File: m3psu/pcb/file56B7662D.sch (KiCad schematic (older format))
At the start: 12 parts

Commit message: Finished passives for Li-ion Charger. Tweaked and cleaned up values in DC/DC Converter.
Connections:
- wire segments 209 -> 164
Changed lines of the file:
@@
 	2250 3600 2200 3600
 Wire Wire Line
-	2250 3300 2250 3400
-Wire Wire Line
-	2250 3400 2250 3500
-Wire Wire Line
-	2250 3500 2250 3600
-Wire Wire Line
-	2250 3600 2250 3700
+	2250 3300 2250 3700
 Wire Wire Line
 	2200 3300 2250 3300
@@
 Connection ~ 950  2400
 Wire Wire Line
-	850  2400 950  2400
-Wire Wire Line
-	950  2400 1000 2400
+	850  2400 1000 2400
 Connection ~ 950  2300
 Wire Wire Line
@@
 	1000 2200 950  2200
 Wire Wire Line
-	950  2100 950  2200
-Wire Wire Line
-	950  2200 950  2300
-Wire Wire Line
-	950  2300 950  2400
-Wire Wire Line
-	950  2400 950  2500
-Wire Wire Line
-	950  2500 950  2600
-Wire Wire Line
-	950  2600 950  2800
+	950  2100 950  2800
 Wire Wire Line
 	950  2600 1000 2600
@@
 	800  3600 1000 3600
 Wire Wire Line
-	800  3350 800  3400
-Wire Wire Line
-	800  3400 800  3600
+	800  3350 800  3600
 Wire Wire Line
 	1000 3400 950  3400
@@
 	800  3100 1000 3100
 Wire Wire Line
-	800  1400 800  1550
-Wire Wire Line
-	800  1550 800  1850
-Wire Wire Line
-	800  1850 800  3100
+	800  1400 800  3100
 Wire Wire Line
 	800  1550 900  1550
@@
 	900  1650 750  1650
 Wire Wire Line
-	750  1500 750  1650
-Wire Wire Line
-	750  1650 750  1900
-Wire Wire Line
-	750  1900 750  2900
-Wire Wire Line
-	750  2900 750  3200
+	750  1500 750  3200
 Wire Wire Line
 	750  3200 1000 3200
@@
 	6750 3600 6700 3600
 Wire Wire Line
-	6750 3300 6750 3400
-Wire Wire Line
-	6750 3400 6750 3500
-Wire Wire Line
-	6750 3500 6750 3600
-Wire Wire Line
-	6750 3600 6750 3700
+	6750 3300 6750 3700
 Wire Wire Line
 	6700 3300 6750 3300
@@
 Connection ~ 5450 2400
 Wire Wire Line
-	5350 2400 5450 2400
-Wire Wire Line
-	5450 2400 5500 2400
+	5350 2400 5500 2400
 Connection ~ 5450 2300
 Wire Wire Line
@@
 	5300 3600 5500 3600
 Wire Wire Line
-	5300 3350 5300 3400
-Wire Wire Line
-	5300 3400 5300 3600
+	5300 3350 5300 3600
 Wire Wire Line
 	5500 3400 5450 3400
@@
 	5300 3100 5500 3100
 Wire Wire Line
-	5300 1400 5300 1550
-Wire Wire Line
-	5300 1550 5300 1850
-Wire Wire Line
-	5300 1850 5300 3100
+	5300 1400 5300 3100
 Wire Wire Line
 	5300 1550 5400 1550
@@
 	5400 1650 5250 1650
 Wire Wire Line
-	5250 1500 5250 1650
-Wire Wire Line
-	5250 1650 5250 1900
-Wire Wire Line
-	5250 1900 5250 2800
-Wire Wire Line
-	5250 2800 5250 2900
-Wire Wire Line
-	5250 2900 5250 3200
+	5250 1500 5250 3200
 Wire Wire Line
 	5250 3200 5500 3200
@@
 	2250 7250 2200 7250
 Wire Wire Line
-	2250 6950 2250 7050
-Wire Wire Line
-	2250 7050 2250 7150
-Wire Wire Line
-	2250 7150 2250 7250
-Wire Wire Line
-	2250 7250 2250 7350
+	2250 6950 2250 7350
 Wire Wire Line
 	2200 6950 2250 6950
@@
 Connection ~ 950  6050
 Wire Wire Line
-	850  6050 950  6050
-Wire Wire Line
-	950  6050 1000 6050
+	850  6050 1000 6050
 Connection ~ 950  5950
 Wire Wire Line
@@
 	1000 5850 950  5850
 Wire Wire Line
-	950  5750 950  5850
-Wire Wire Line
-	950  5850 950  5950
-Wire Wire Line
-	950  5950 950  6050
-Wire Wire Line
-	950  6050 950  6150
-Wire Wire Line
-	950  6150 950  6250
-Wire Wire Line
-	950  6250 950  6450
+	950  5750 950  6450
 Wire Wire Line
 	800  7250 1000 7250
 Wire Wire Line
-	800  7000 800  7050
-Wire Wire Line
-	800  7050 800  7250
+	800  7000 800  7250
 Wire Wire Line
 	1000 7050 950  7050
@@
 	800  6750 1000 6750
 Wire Wire Line
-	800  5050 800  5200
-Wire Wire Line
-	800  5200 800  5500
-Wire Wire Line
-	800  5500 800  6750
+	800  5050 800  6750
 Wire Wire Line
 	800  5200 900  5200
@@
 	900  5300 750  5300
 Wire Wire Line
-	750  5150 750  5300
-Wire Wire Line
-	750  5300 750  5550
-Wire Wire Line
-	750  5550 750  6550
-Wire Wire Line
-	750  6550 750  6850
+	750  5150 750  6850
 Wire Wire Line
 	750  6850 1000 6850
@@
 	850  6250 850  6200
 Wire Wire Line
-	5450 2100 5450 2200
-Wire Wire Line
-	5450 2200 5450 2300
-Wire Wire Line
-	5450 2300 5450 2400
-Wire Wire Line
-	5450 2400 5450 2500
-Wire Wire Line
-	5450 2500 5450 2600
+	5450 2100 5450 2600
 Wire Wire Line
 	5500 2800 5250 2800

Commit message: Linked the footprints to some parts. Cleaned up a little more of DC/DC Converter.
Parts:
- R? (x3): value 1K -> 1k
- R? (x3): value 100K -> 10k
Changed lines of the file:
@@
 P 850 3400
 F 0 "R?" H 900 3450 50  0000 C CNN
-F 1 "1K" H 900 3350 50  0000 C CNN
+F 1 "1k" H 900 3350 50  0000 C CNN
 F 2 "" H 850 3400 50  0001 C CNN
 F 3 "" H 850 3400 50  0001 C CNN
@@
 P 2250 2200
 F 0 "R?" H 2300 2250 50  0000 C CNN
-F 1 "100K" H 2300 2150 50  0000 C CNN
+F 1 "10k" H 2300 2150 50  0000 C CNN
 F 2 "" H 2250 2200 50  0001 C CNN
 F 3 "" H 2250 2200 50  0001 C CNN
@@
 P 5350 3400
 F 0 "R?" H 5400 3450 50  0000 C CNN
-F 1 "1K" H 5400 3350 50  0000 C CNN
+F 1 "1k" H 5400 3350 50  0000 C CNN
 F 2 "" H 5350 3400 50  0001 C CNN
 F 3 "" H 5350 3400 50  0001 C CNN
@@
 P 6750 2200
 F 0 "R?" H 6800 2250 50  0000 C CNN
-F 1 "100K" H 6800 2150 50  0000 C CNN
+F 1 "10k" H 6800 2150 50  0000 C CNN
 F 2 "" H 6750 2200 50  0001 C CNN
 F 3 "" H 6750 2200 50  0001 C CNN
@@
 P 850 7050
 F 0 "R?" H 900 7100 50  0000 C CNN
-F 1 "1K" H 900 7000 50  0000 C CNN
+F 1 "1k" H 900 7000 50  0000 C CNN
 F 2 "" H 850 7050 50  0001 C CNN
 F 3 "" H 850 7050 50  0001 C CNN
@@
 P 2250 5850
 F 0 "R?" H 2300 5900 50  0000 C CNN
-F 1 "100K" H 2300 5800 50  0000 C CNN
+F 1 "10k" H 2300 5800 50  0000 C CNN
 F 2 "" H 2250 5850 50  0001 C CNN
 F 3 "" H 2250 5850 50  0001 C CNN

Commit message: Finished touchup. All components have Farnell Numbers. Need help for creating A/B footprints before routing can begin.
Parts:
- removed C? (x2): 100n, symbol C
- removed R? (x2): 1k, symbol R
- removed R? (x2): 10k, symbol R
- added C? (x2): 100n, agg:0402, symbol C
- added R? (x2): 4k7, agg:0402, symbol R
- added R? (x2): 1k, agg:0402, symbol R
- added R? (x2): 10k, agg:0402, symbol R
- C?: footprint (none) -> agg:0402; Farnell (none) -> 2496811
- R?: footprint (none) -> agg:0402; Farnell (none) -> 2447120
- R?: footprint (none) -> agg:0402; Farnell (none) -> 2447096
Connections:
- wire segments 164 -> 218

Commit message: Added address text to Li-ion Charger. Updated README.md.
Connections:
- wire segments 218 -> 170
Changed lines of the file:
@@
 	2250 3600 2200 3600
 Wire Wire Line
-	2250 3300 2250 3400
-Wire Wire Line
-	2250 3400 2250 3500
-Wire Wire Line
-	2250 3500 2250 3600
-Wire Wire Line
-	2250 3600 2250 3700
+	2250 3300 2250 3700
 Wire Wire Line
 	2200 3300 2250 3300
@@
 Connection ~ 950  2400
 Wire Wire Line
-	850  2400 950  2400
-Wire Wire Line
-	950  2400 1000 2400
+	850  2400 1000 2400
 Connection ~ 950  2300
 Wire Wire Line
@@
 	1000 2200 950  2200
 Wire Wire Line
-	950  2100 950  2200
-Wire Wire Line
-	950  2200 950  2300
-Wire Wire Line
-	950  2300 950  2400
-Wire Wire Line
-	950  2400 950  2500
-Wire Wire Line
-	950  2500 950  2600
-Wire Wire Line
-	950  2600 950  2800
+	950  2100 950  2800
 Wire Wire Line
 	950  2600 1000 2600
@@
 	800  3600 1000 3600
 Wire Wire Line
-	800  3350 800  3400
-Wire Wire Line
-	800  3400 800  3600
+	800  3350 800  3600
 Wire Wire Line
 	1000 3400 950  3400
@@
 	800  3100 1000 3100
 Wire Wire Line
-	800  1400 800  1550
-Wire Wire Line
-	800  1550 800  1850
-Wire Wire Line
-	800  1850 800  3100
+	800  1400 800  3100
 Wire Wire Line
 	800  1550 900  1550
@@
 	900  1650 750  1650
 Wire Wire Line
-	750  1500 750  1650
-Wire Wire Line
-	750  1650 750  1900
-Wire Wire Line
-	750  1900 750  2900
-Wire Wire Line
-	750  2900 750  3200
+	750  1500 750  3200
 Wire Wire Line
 	750  3200 1000 3200
@@
 	6750 3600 6700 3600
 Wire Wire Line
-	6750 3300 6750 3400
-Wire Wire Line
-	6750 3400 6750 3500
-Wire Wire Line
-	6750 3500 6750 3600
-Wire Wire Line
-	6750 3600 6750 3700
+	6750 3300 6750 3700
 Wire Wire Line
 	6700 3300 6750 3300
@@
 Connection ~ 5450 2400
 Wire Wire Line
-	5350 2400 5450 2400
-Wire Wire Line
-	5450 2400 5500 2400
+	5350 2400 5500 2400
 Connection ~ 5450 2300
 Wire Wire Line
@@
 	5300 3600 5500 3600
 Wire Wire Line
-	5300 3350 5300 3400
-Wire Wire Line
-	5300 3400 5300 3600
+	5300 3350 5300 3600
 Wire Wire Line
 	5500 3400 5450 3400
@@
 	5300 3100 5500 3100
 Wire Wire Line
-	5300 1400 5300 1550
-Wire Wire Line
-	5300 1550 5300 1850
-Wire Wire Line
-	5300 1850 5300 3100
+	5300 1400 5300 3100
 Wire Wire Line
 	5300 1550 5400 1550
@@
 	5400 1650 5250 1650
 Wire Wire Line
-	5250 1500 5250 1650
-Wire Wire Line
-	5250 1650 5250 1900
-Wire Wire Line
-	5250 1900 5250 2800
-Wire Wire Line
-	5250 2800 5250 2900
-Wire Wire Line
-	5250 2900 5250 3200
+	5250 1500 5250 3200
 Wire Wire Line
 	5250 3200 5500 3200
@@
 	2250 7250 2200 7250
 Wire Wire Line
-	2250 6950 2250 7050
-Wire Wire Line
-	2250 7050 2250 7150
-Wire Wire Line
-	2250 7150 2250 7250
-Wire Wire Line
-	2250 7250 2250 7350
+	2250 6950 2250 7350
 Wire Wire Line
 	2200 6950 2250 6950
@@
 Connection ~ 950  6050
 Wire Wire Line
-	850  6050 950  6050
-Wire Wire Line
-	950  6050 1000 6050
+	850  6050 1000 6050
 Connection ~ 950  5950
 Wire Wire Line
@@
 	1000 5850 950  5850
 Wire Wire Line
-	950  5750 950  5850
-Wire Wire Line
-	950  5850 950  5950
-Wire Wire Line
-	950  5950 950  6050
-Wire Wire Line
-	950  6050 950  6150
-Wire Wire Line
-	950  6150 950  6250
-Wire Wire Line
-	950  6250 950  6450
+	950  5750 950  6450
 Wire Wire Line
 	800  7250 1000 7250
 Wire Wire Line
-	800  7000 800  7050
-Wire Wire Line
-	800  7050 800  7250
+	800  7000 800  7250
 Wire Wire Line
 	1000 7050 950  7050
@@
 	800  6750 1000 6750
 Wire Wire Line
-	800  5050 800  5200
-Wire Wire Line
-	800  5200 800  5500
-Wire Wire Line
-	800  5500 800  6750
+	800  5050 800  6750
 Wire Wire Line
 	800  5200 900  5200
@@
 	900  5300 750  5300
 Wire Wire Line
-	750  5150 750  5300
-Wire Wire Line
-	750  5300 750  5550
-Wire Wire Line
-	750  5550 750  6550
-Wire Wire Line
-	750  6550 750  6850
+	750  5150 750  6850
 Wire Wire Line
 	750  6850 1000 6850
@@
 	850  6250 850  6200
 Wire Wire Line
-	5450 2100 5450 2200
-Wire Wire Line
-	5450 2200 5450 2300
-Wire Wire Line
-	5450 2300 5450 2400
-Wire Wire Line
-	5450 2400 5450 2500
-Wire Wire Line
-	5450 2500 5450 2600
+	5450 2100 5450 2600
 Wire Wire Line
 	5500 2800 5250 2800
@@
 	950  6250 1000 6250
 Wire Wire Line
-	5500 4800 5850 4800
-Wire Wire Line
-	5850 4800 5950 4800
-Wire Wire Line
-	5950 4900 5650 4900
-Wire Wire Line
-	5650 4900 5500 4900
+	5500 4800 5950 4800
+Wire Wire Line
+	5500 4900 5950 4900
 Connection ~ 800  5200
 Connection ~ 750  5300
@@
 $EndComp
 Wire Wire Line
-	5850 4600 5750 4600
-Wire Wire Line
-	5750 4600 5650 4600
+	5650 4600 5850 4600
 Wire Wire Line
 	5650 4600 5650 4650

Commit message: Added current monitor and control for pyros. Modified DC/DC converters.
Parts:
- removed C? (x3): 100n, agg:0402, symbol C
- removed IC? (x3): PCA9502, agg:HVQFN24-NXP, symbol PCA9502
- removed R? (x3): 1k, agg:0402, symbol R
- removed R? (x3): 10k, agg:0402, symbol R
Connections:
- net labels removed: GND
- wire segments 170 -> 44
- no-connect marks 15 -> 0
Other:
- note removed: "Address 0x50\n(0xA0 on datasheet)"
- note removed: "Address 0x52\n(0xA4 on datasheet)"
- note removed: "Address 0x54\n(0xA8 on datasheet)"
- moved on the sheet: R?

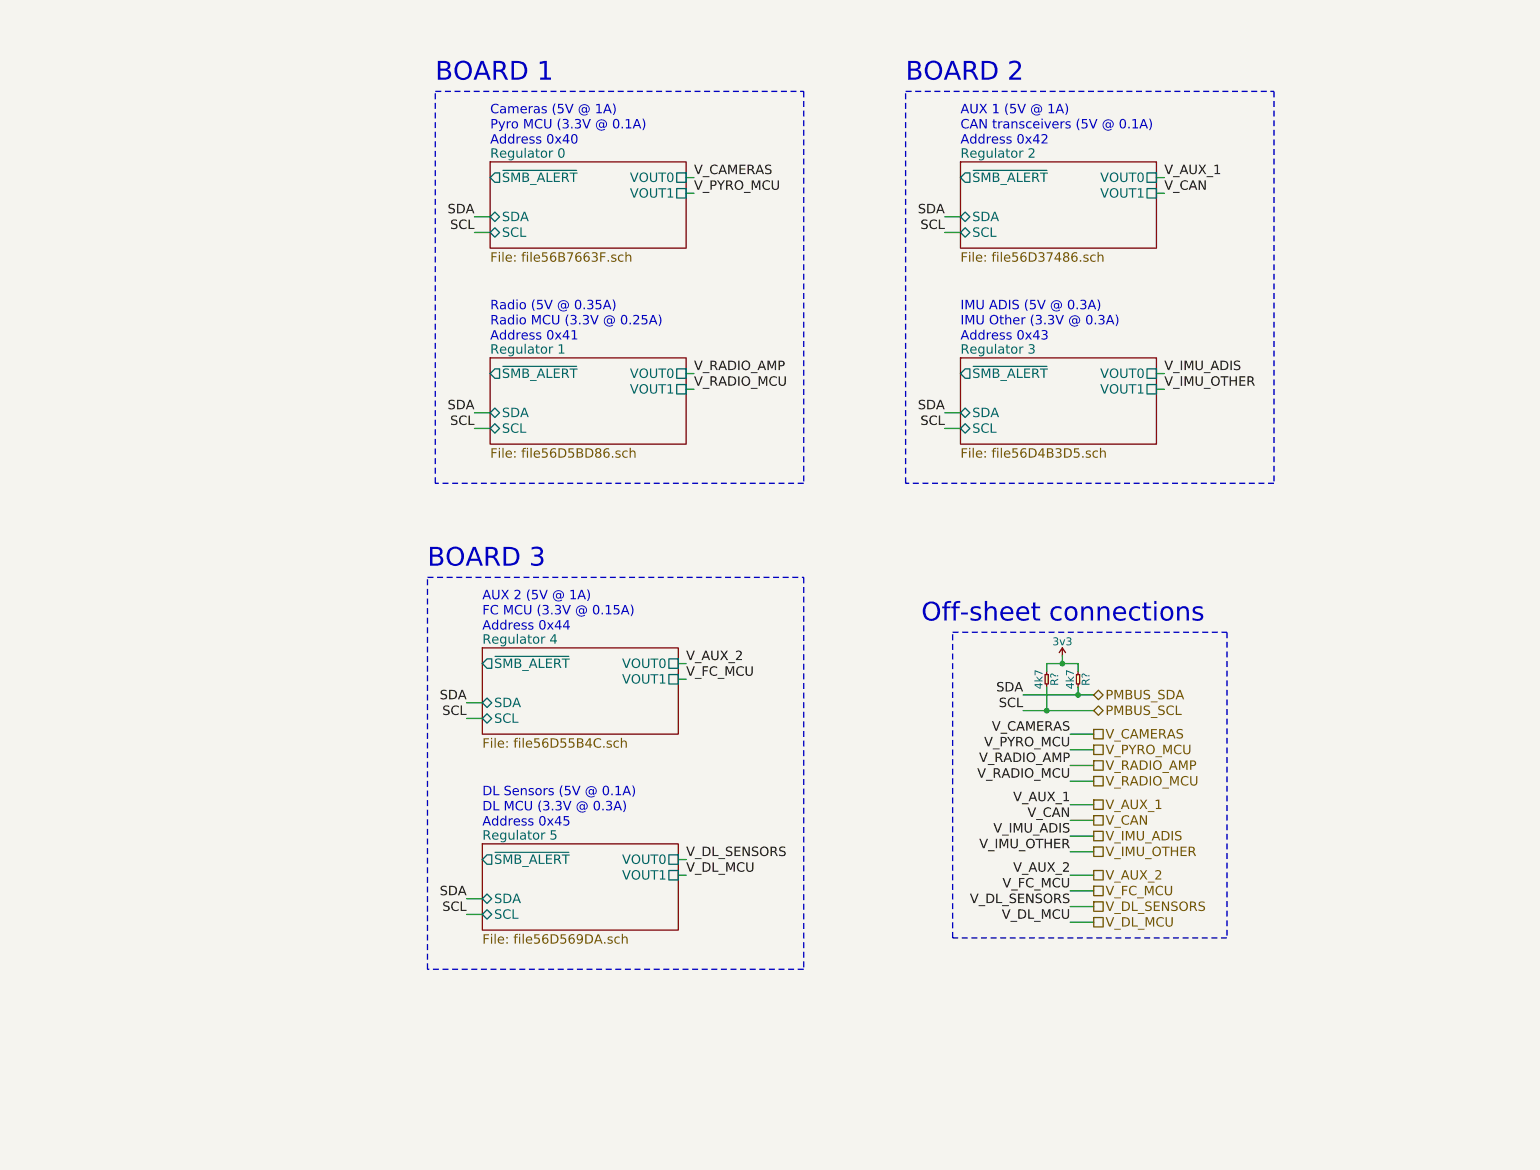
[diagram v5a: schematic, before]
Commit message: Changes in arrangement of schematic. Started wiring interconnects. WIP.
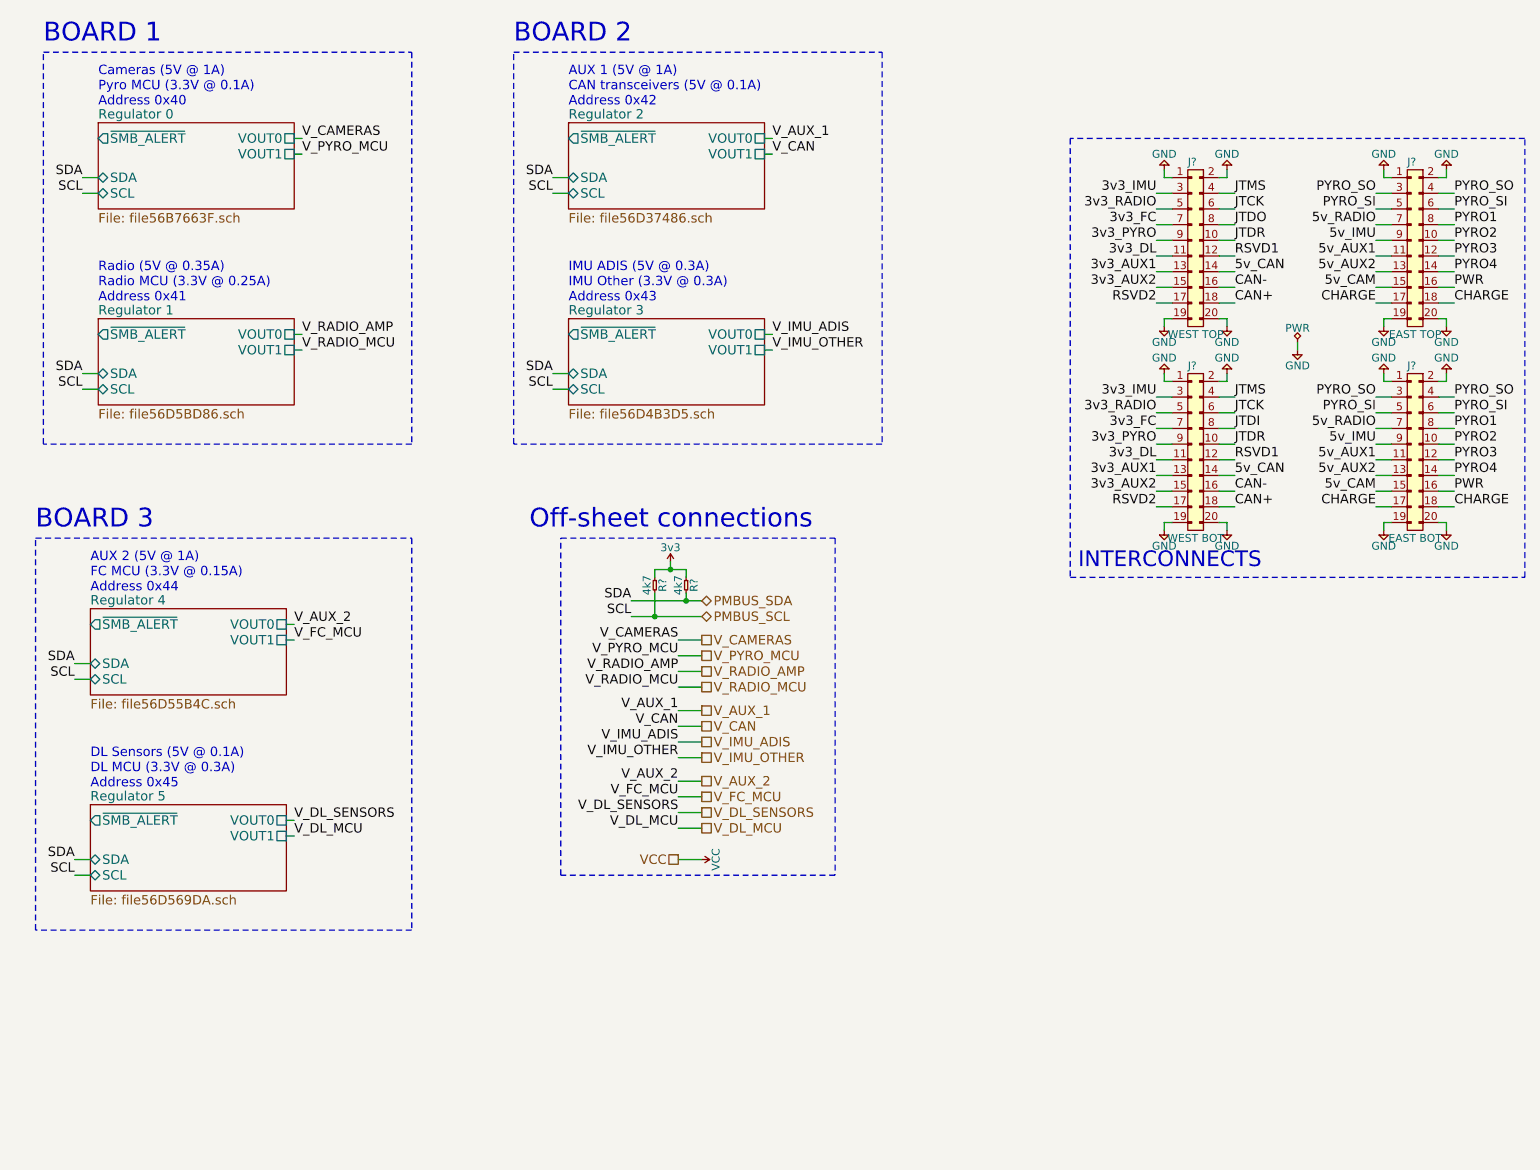
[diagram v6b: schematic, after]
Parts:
- added J?: WEST TOP, symbol CONN_02x10
- added J?: EAST TOP, symbol CONN_02x10
- added J?: WEST BOT, symbol CONN_02x10
- added J?: EAST BOT, symbol CONN_02x10
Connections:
- new net 3v3_AUX1: J?.13, J?.13
- new net 3v3_AUX2: J?.15, J?.15
- new net 3v3_DL: J?.11, J?.11
- new net 3v3_FC: J?.7, J?.7
- new net 3v3_IMU: J?.3, J?.3
- new net 3v3_PYRO: J?.9, J?.9
- new net 3v3_RADIO: J?.5, J?.5
- new net 5v_AUX1: J?.11, J?.11
- new net 5v_AUX2: J?.13, J?.13
- new net 5v_CAM: J?.15, J?.15
- new net 5v_CAN: J?.14, J?.14
- new net 5v_IMU: J?.9, J?.9
- new net 5v_RADIO: J?.7, J?.7
- new net CAN+: J?.18, J?.18
- new net CAN-: J?.16, J?.16
- new net CHARGE: J?.17, J?.17, J?.18, J?.18
- new net GND: J?.1, J?.1, J?.1, J?.1, J?.19, J?.19, J?.19, J?.19, J?.2, J?.2, J?.2, J?.2, J?.20, J?.20, J?.20, J?.20
- new net JTCK: J?.6, J?.6
- new net JTDI: J?.8
- new net JTDO: J?.8
- new net JTDR: J?.10, J?.10
- new net JTMS: J?.4, J?.4
- new net PWR: J?.16, J?.16
- new net PYRO1: J?.8, J?.8
- new net PYRO2: J?.10, J?.10
- new net PYRO3: J?.12, J?.12
- new net PYRO4: J?.14, J?.14
- new net PYRO_SI: J?.5, J?.5, J?.6, J?.6
- new net PYRO_SO: J?.3, J?.3, J?.4, J?.4
- new net RSVD1: J?.12, J?.12
- new net RSVD2: J?.17, J?.17
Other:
- note added: "INTERCONNECTS"
- moved on the sheet: R?
